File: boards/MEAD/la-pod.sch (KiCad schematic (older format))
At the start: 22 parts, among them J1 CONN_SFF8087

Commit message: Continued MEAD layout
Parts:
- removed TP4: TESTPAD, azonenberg_pcb:TESTPOINT_SMT_0.5MM, symbol Connector:Conn_01x01
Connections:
- net GND: now also TP12.1 (Pin_1)
- net TX0_N: now also J1.B2 (TX0_P); no longer J1.B3 (TX0_N)
- net TX0_P: now also J1.B3 (TX0_N); no longer J1.B2 (TX0_P)
- net TX1_N: now also D2.1 (IO1); no longer D2.3 (IO2)
- net TX1_P: now also D2.3 (IO2); no longer D2.1 (IO1)
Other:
- note added: "Invert lanes 0 for routability"
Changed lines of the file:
@@
 Text Label 4800 2600 2    50   ~ 0
 5V0
-Wire Wire Line
-	7700 1200 8250 1200
-Wire Wire Line
-	7700 1300 8250 1300
 $Comp
 L special-azonenberg:SP4010 D1
@@
 Wire Wire Line
 	7700 1600 8250 1600
-Text Label 7800 1200 0    50   ~ 0
+Text Label 7700 1200 0    50   ~ 0
 TX0_P
-Text Label 7800 1300 0    50   ~ 0
+Text Label 7700 1300 0    50   ~ 0
 TX0_N
 Text Label 7800 1500 0    50   ~ 0
@@
 	1    0    0    -1
 $EndComp
+Text Label 900  7450 2    50   ~ 0
+TX1_P
 Text Label 900  7350 2    50   ~ 0
-TX1_P
-Text Label 900  7450 2    50   ~ 0
 TX1_N
 Text Label 900  6850 2    50   ~ 0
@@
 	1    0    0    -1
 $EndComp
-Text Label 9700 5400 2    50   ~ 0
-GND
-$Comp
-L Connector:Conn_01x01 TP4
-U 1 1 5ED5A825
-P 8950 5200
-F 0 "TP4" H 9030 5242 50  0000 L CNN
-F 1 "TESTPAD" H 9030 5151 50  0000 L CNN
-F 2 "azonenberg_pcb:TESTPOINT_SMT_0.5MM" H 8950 5200 50  0001 C CNN
-F 3 "~" H 8950 5200 50  0001 C CNN
-	1    8950 5200
-	1    0    0    -1
-$EndComp
-Text Label 8750 5200 2    50   ~ 0
-12V0
+Text Label 9700 5450 2    50   ~ 0
+GND
 $Comp
 L Connector:Conn_01x01 TP5
@@
 	1    0    0    -1
 $EndComp
+Text Label 8250 1300 2    50   ~ 0
+TX0_P
+Text Label 8250 1200 2    50   ~ 0
+TX0_N
+Text Notes 8350 1100 0    50   ~ 0
+Invert lanes 0 for routability
 $EndSCHEMATC

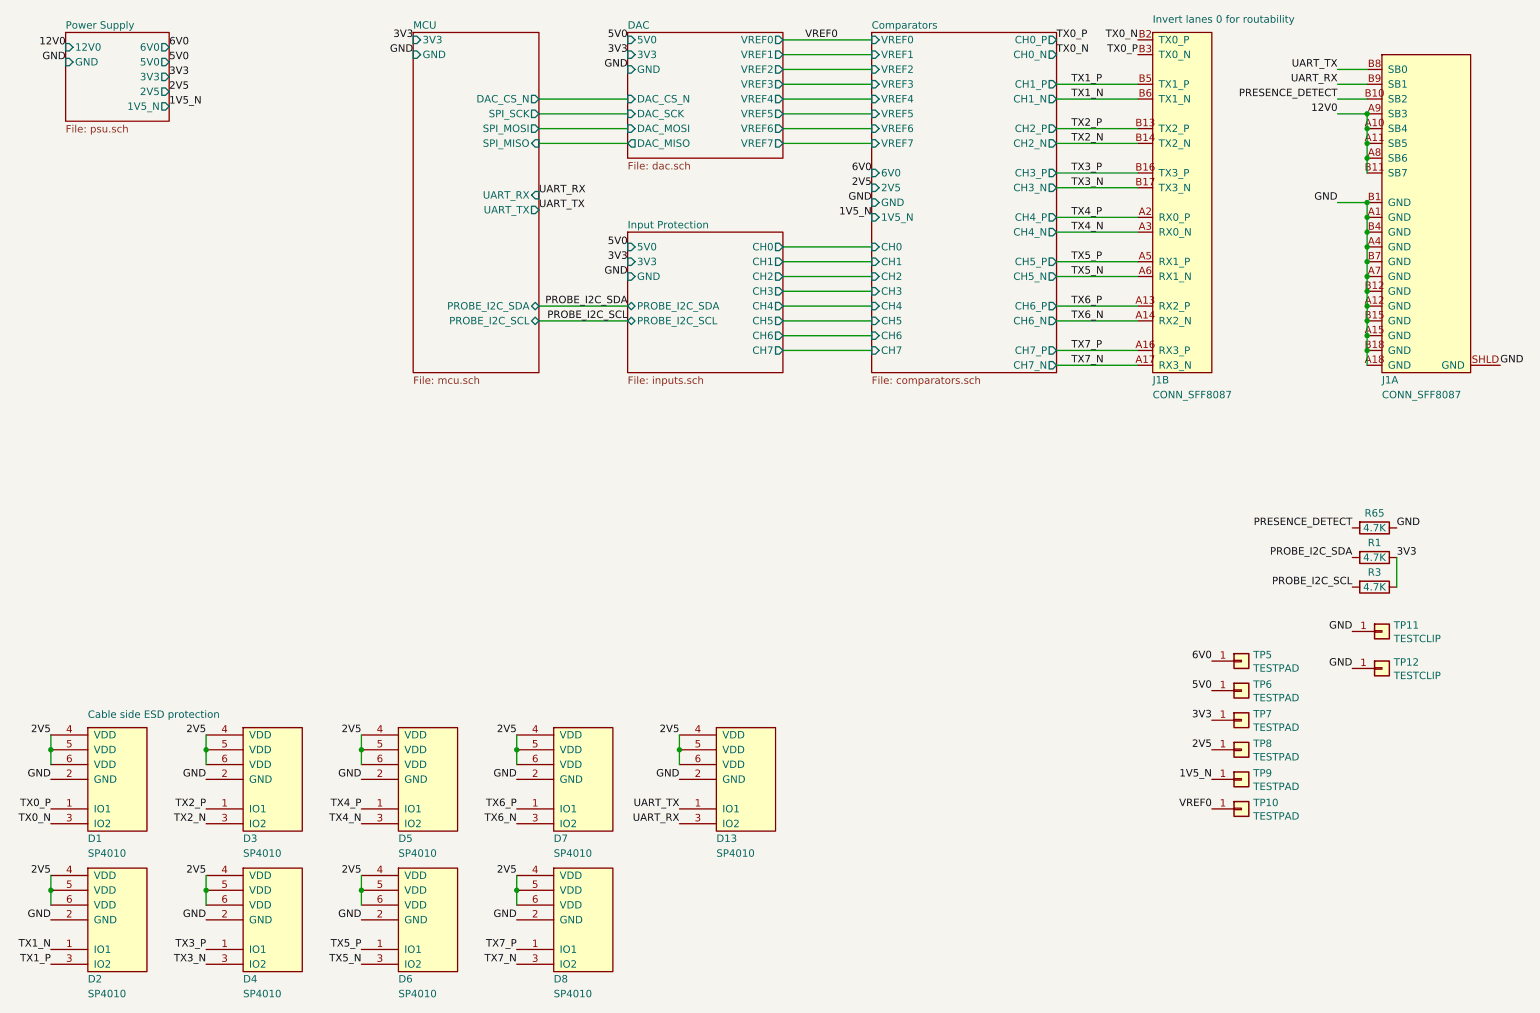
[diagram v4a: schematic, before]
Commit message: Continued MEAD layout. Right side is almost done.
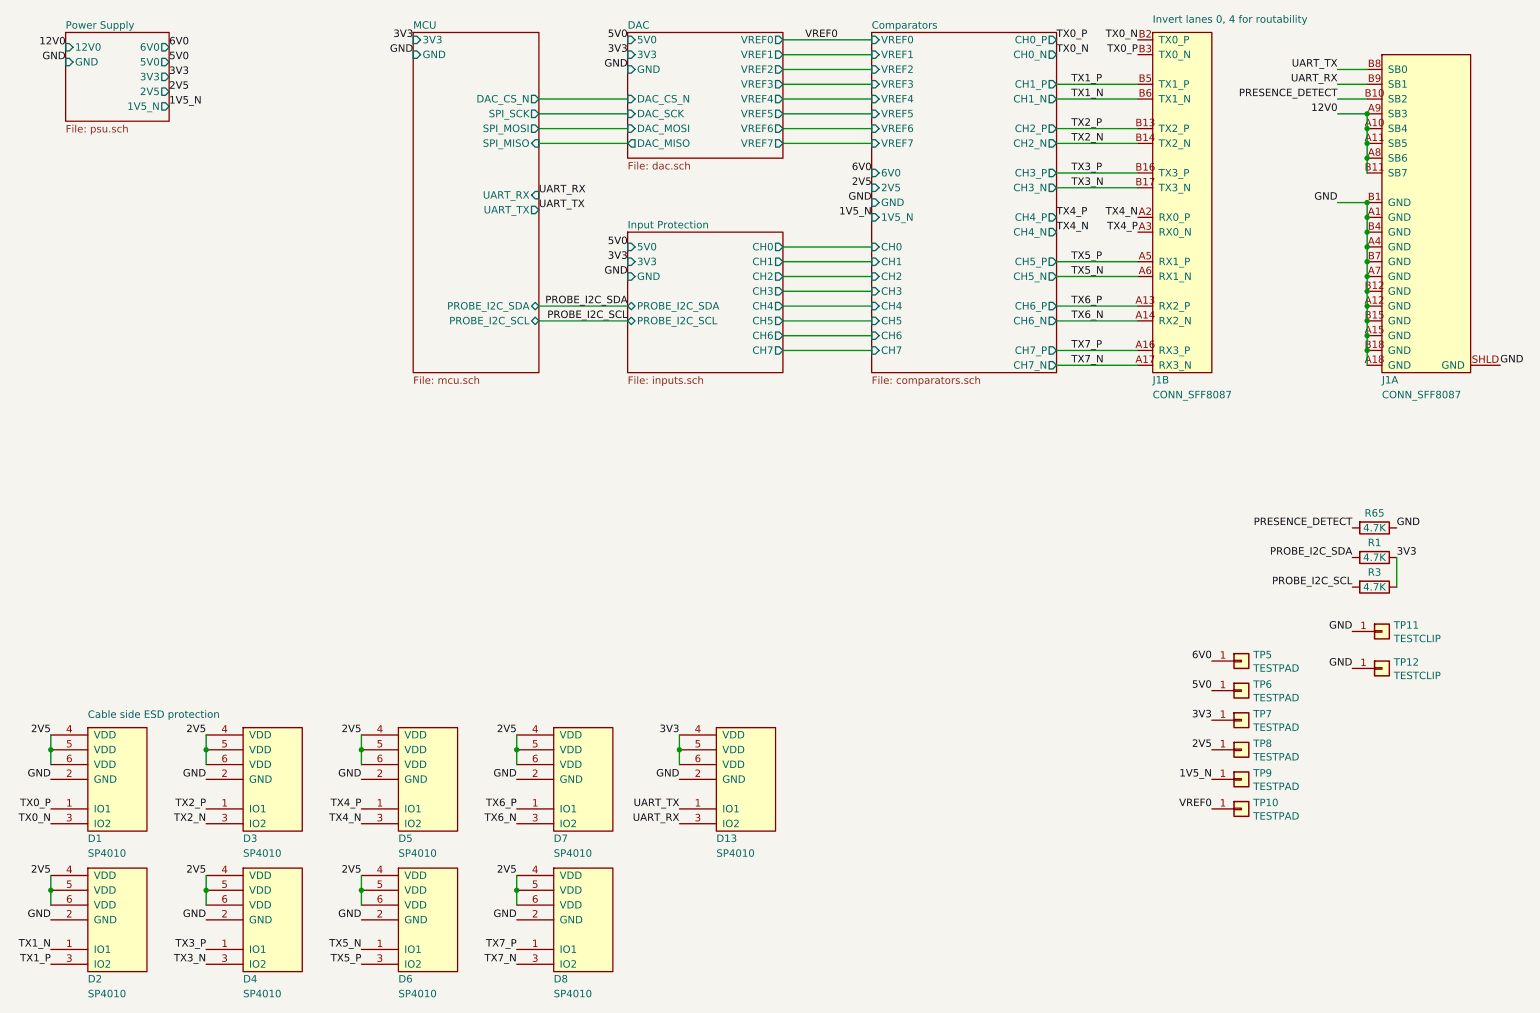
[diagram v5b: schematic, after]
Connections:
- net 2V5: no longer D13.4 (VDD), D13.5 (VDD), D13.6 (VDD)
- net 3V3: now also D13.4 (VDD), D13.5 (VDD), D13.6 (VDD)
- net TX4_N: now also J1.A2 (RX0_P); no longer J1.A3 (RX0_N)
- net TX4_P: now also J1.A3 (RX0_N); no longer J1.A2 (RX0_P)
- net TX5_N: now also D6.1 (IO1); no longer D6.3 (IO2)
- net TX5_P: now also D6.3 (IO2); no longer D6.1 (IO1)
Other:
- note added: "Invert lanes 0, 4 for routability"
- note removed: "Invert lanes 0 for routability"
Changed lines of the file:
@@
 Wire Wire Line
 	7700 2200 8250 2200
-Text Label 7800 2400 0    50   ~ 0
+Text Label 7700 2400 0    50   ~ 0
 TX4_P
-Text Label 7800 2500 0    50   ~ 0
+Text Label 7700 2500 0    50   ~ 0
 TX4_N
-Wire Wire Line
-	7700 2400 8250 2400
-Wire Wire Line
-	7700 2500 8250 2500
 Text Label 7800 2700 0    50   ~ 0
 TX5_P
@@
 	1    0    0    -1
 $EndComp
+Text Label 3000 7450 2    50   ~ 0
+TX5_P
 Text Label 3000 7350 2    50   ~ 0
-TX5_P
-Text Label 3000 7450 2    50   ~ 0
 TX5_N
 Text Label 3000 6850 2    50   ~ 0
@@
 $EndComp
 Text Label 5150 5900 2    50   ~ 0
-2V5
+3V3
 Wire Wire Line
 	5150 5900 5150 6000
@@
 TX0_N
 Text Notes 8350 1100 0    50   ~ 0
-Invert lanes 0 for routability
+Invert lanes 0, 4 for routability
+Text Label 8250 2500 2    50   ~ 0
+TX4_P
+Text Label 8250 2400 2    50   ~ 0
+TX4_N
 $EndSCHEMATC

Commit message: Finished MCU layout, began left side comparator layout.
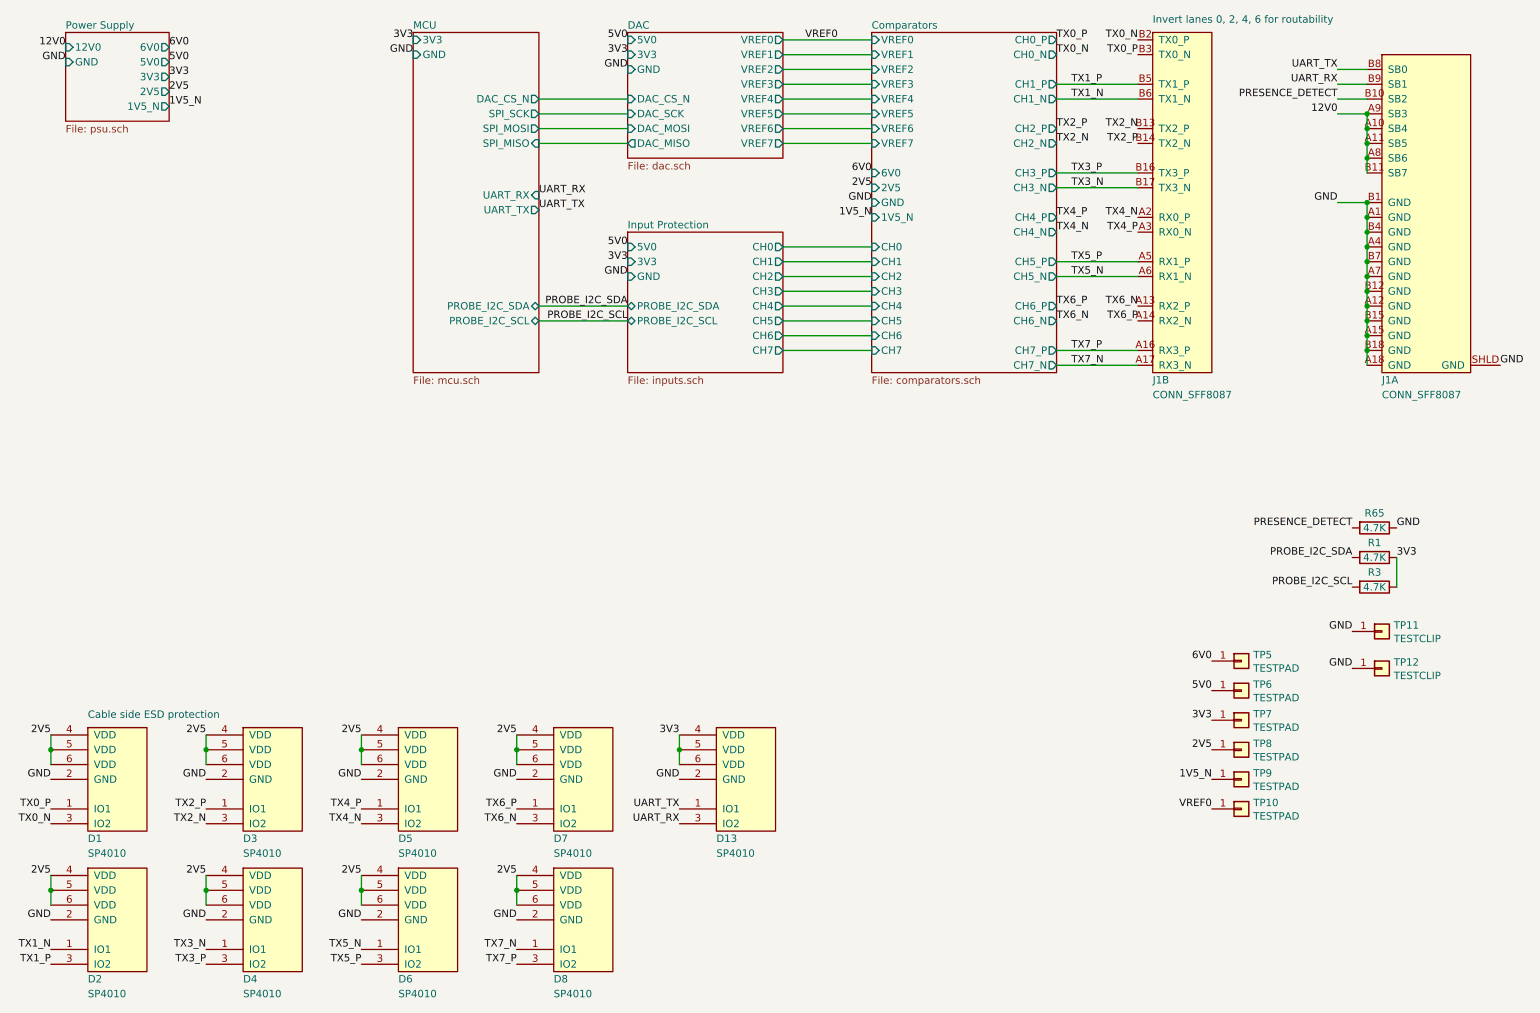
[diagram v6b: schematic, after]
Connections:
- net TX2_N: now also J1.B13 (TX2_P); no longer J1.B14 (TX2_N)
- net TX2_P: now also J1.B14 (TX2_N); no longer J1.B13 (TX2_P)
- net TX3_N: now also D4.1 (IO1); no longer D4.3 (IO2)
- net TX3_P: now also D4.3 (IO2); no longer D4.1 (IO1)
- net TX6_N: now also J1.A13 (RX2_P); no longer J1.A14 (RX2_N)
- net TX6_P: now also J1.A14 (RX2_N); no longer J1.A13 (RX2_P)
- net TX7_N: now also D8.1 (IO1); no longer D8.3 (IO2)
- net TX7_P: now also D8.3 (IO2); no longer D8.1 (IO1)
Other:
- note added: "Invert lanes 0, 2, 4, 6 for routability"
- note removed: "Invert lanes 0, 4 for routability"
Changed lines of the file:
@@
 	1    0    0    -1
 $EndComp
-Wire Wire Line
-	7700 1500 8250 1500
-Wire Wire Line
-	7700 1600 8250 1600
 Text Label 7700 1200 0    50   ~ 0
 TX0_P
@@
 Text Label 7800 1600 0    50   ~ 0
 TX1_N
-Text Label 7800 1800 0    50   ~ 0
+Text Label 7700 1800 0    50   ~ 0
 TX2_P
-Text Label 7800 1900 0    50   ~ 0
+Text Label 7700 1900 0    50   ~ 0
 TX2_N
 Text Label 7800 2100 0    50   ~ 0
@@
 Text Label 7800 2200 0    50   ~ 0
 TX3_N
-Wire Wire Line
-	7700 1800 8250 1800
-Wire Wire Line
-	7700 1900 8250 1900
-Wire Wire Line
-	7700 2100 8250 2100
-Wire Wire Line
-	7700 2200 8250 2200
 Text Label 7700 2400 0    50   ~ 0
 TX4_P
@@
 Wire Wire Line
 	7700 2800 8250 2800
-Text Label 7800 3000 0    50   ~ 0
+Text Label 7700 3000 0    50   ~ 0
 TX6_P
-Text Label 7800 3100 0    50   ~ 0
+Text Label 7700 3100 0    50   ~ 0
 TX6_N
-Wire Wire Line
-	7700 3000 8250 3000
-Wire Wire Line
-	7700 3100 8250 3100
 Text Label 7800 3300 0    50   ~ 0
 TX7_P
@@
 	1    0    0    -1
 $EndComp
+Text Label 1950 7450 2    50   ~ 0
+TX3_P
 Text Label 1950 7350 2    50   ~ 0
-TX3_P
-Text Label 1950 7450 2    50   ~ 0
 TX3_N
 Text Label 1950 6850 2    50   ~ 0
@@
 	1    0    0    -1
 $EndComp
+Text Label 4050 7450 2    50   ~ 0
+TX7_P
 Text Label 4050 7350 2    50   ~ 0
-TX7_P
-Text Label 4050 7450 2    50   ~ 0
 TX7_N
 Text Label 4050 6850 2    50   ~ 0
@@
 TX0_N
 Text Notes 8350 1100 0    50   ~ 0
-Invert lanes 0, 4 for routability
+Invert lanes 0, 2, 4, 6 for routability
 Text Label 8250 2500 2    50   ~ 0
 TX4_P
 Text Label 8250 2400 2    50   ~ 0
 TX4_N
+Wire Wire Line
+	7700 1600 8250 1600
+Wire Wire Line
+	7700 1500 8250 1500
+Text Label 8250 3100 2    50   ~ 0
+TX6_P
+Text Label 8250 3000 2    50   ~ 0
+TX6_N
+Text Label 8250 1900 2    50   ~ 0
+TX2_P
+Text Label 8250 1800 2    50   ~ 0
+TX2_N
+Wire Wire Line
+	7700 2100 8250 2100
+Wire Wire Line
+	7700 2200 8250 2200
 $EndSCHEMATC

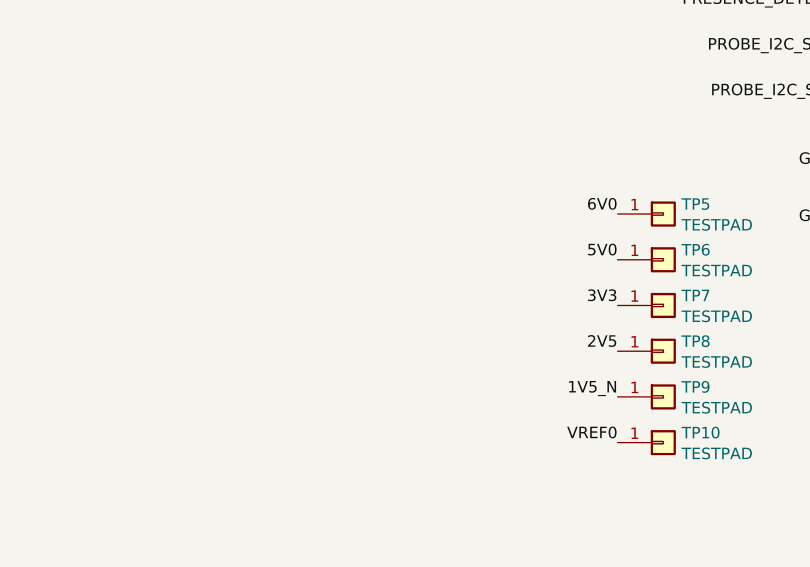
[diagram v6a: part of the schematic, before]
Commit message: Continued layout on MEAD. All comparators done, LVDS length matched, DAC routed
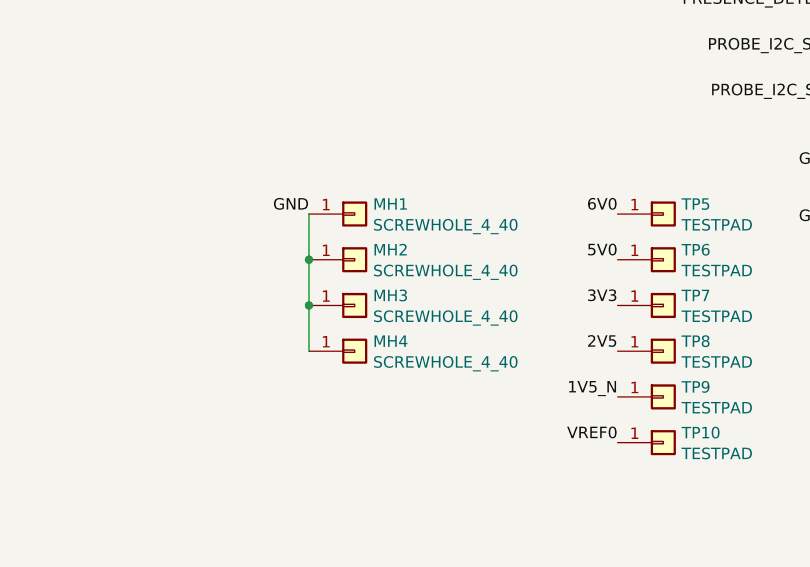
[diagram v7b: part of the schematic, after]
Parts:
- added MH1, MH2, MH3, MH4: SCREWHOLE_4_40, azonenberg_pcb:MECHANICAL_CLEARANCEHOLE_4_40, symbol Connector:Conn_01x01
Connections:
- net GND: now also MH1.1 (Pin_1), MH2.1 (Pin_1), MH3.1 (Pin_1), MH4.1 (Pin_1)
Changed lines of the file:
@@
 Wire Wire Line
 	7700 2200 8250 2200
+$Comp
+L Connector:Conn_01x01 MH1
+U 1 1 5F2DE5BB
+P 7600 5400
+F 0 "MH1" H 7680 5442 50  0000 L CNN
+F 1 "SCREWHOLE_4_40" H 7680 5351 50  0000 L CNN
+F 2 "azonenberg_pcb:MECHANICAL_CLEARANCEHOLE_4_40" H 7600 5400 50  0001 C CNN
+F 3 "~" H 7600 5400 50  0001 C CNN
+	1    7600 5400
+	1    0    0    -1
+$EndComp
+Text Label 7400 5400 2    50   ~ 0
+GND
+$Comp
+L Connector:Conn_01x01 MH2
+U 1 1 5F2DF305
+P 7600 5600
+F 0 "MH2" H 7680 5642 50  0000 L CNN
+F 1 "SCREWHOLE_4_40" H 7680 5551 50  0000 L CNN
+F 2 "azonenberg_pcb:MECHANICAL_CLEARANCEHOLE_4_40" H 7600 5600 50  0001 C CNN
+F 3 "~" H 7600 5600 50  0001 C CNN
+	1    7600 5600
+	1    0    0    -1
+$EndComp
+$Comp
+L Connector:Conn_01x01 MH3
+U 1 1 5F2DF699
+P 7600 5800
+F 0 "MH3" H 7680 5842 50  0000 L CNN
+F 1 "SCREWHOLE_4_40" H 7680 5751 50  0000 L CNN
+F 2 "azonenberg_pcb:MECHANICAL_CLEARANCEHOLE_4_40" H 7600 5800 50  0001 C CNN
+F 3 "~" H 7600 5800 50  0001 C CNN
+	1    7600 5800
+	1    0    0    -1
+$EndComp
+$Comp
+L Connector:Conn_01x01 MH4
+U 1 1 5F2DFA38
+P 7600 6000
+F 0 "MH4" H 7680 6042 50  0000 L CNN
+F 1 "SCREWHOLE_4_40" H 7680 5951 50  0000 L CNN
+F 2 "azonenberg_pcb:MECHANICAL_CLEARANCEHOLE_4_40" H 7600 6000 50  0001 C CNN
+F 3 "~" H 7600 6000 50  0001 C CNN
+	1    7600 6000
+	1    0    0    -1
+$EndComp
+Wire Wire Line
+	7400 6000 7400 5800
+Connection ~ 7400 5600
+Wire Wire Line
+	7400 5600 7400 5400
+Connection ~ 7400 5800
+Wire Wire Line
+	7400 5800 7400 5600
 $EndSCHEMATC

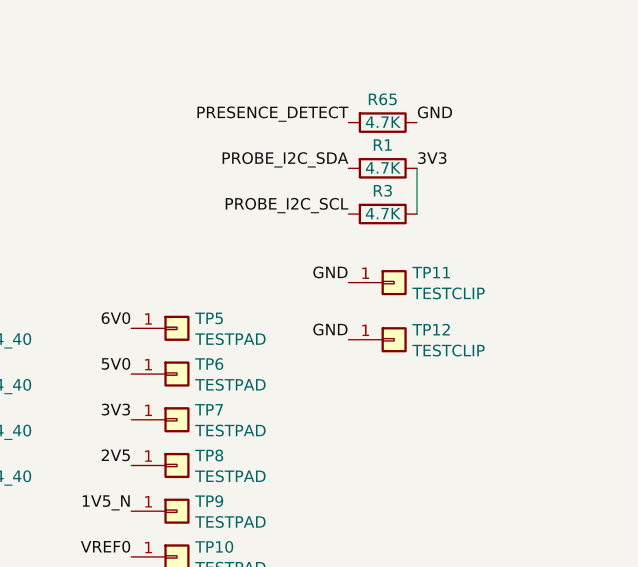
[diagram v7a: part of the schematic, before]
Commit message: Updating file: la-pod.kicad_pcb with current fully routed design
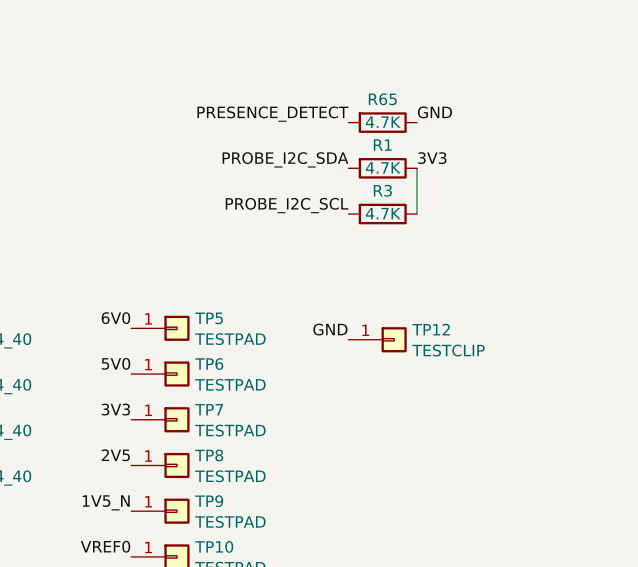
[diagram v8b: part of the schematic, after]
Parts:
- removed TP11: TESTCLIP, azonenberg_pcb:TESTPOINT_SMT_KEYSTONE_5016, symbol Connector:Conn_01x01
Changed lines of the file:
@@
 Sheet 1 6
 Title "Logic Analyzer Pod"
-Date "2020-05-29"
+Date "2020-05-30"
 Rev "0.1"
 Comp "Antikernel Labs"
@@
 UART_RX
 $Comp
-L Connector:Conn_01x01 TP11
-U 1 1 5ED596F2
-P 9900 5200
-F 0 "TP11" H 9980 5242 50  0000 L CNN
-F 1 "TESTCLIP" H 9980 5151 50  0000 L CNN
-F 2 "azonenberg_pcb:TESTPOINT_SMT_KEYSTONE_5016" H 9900 5200 50  0001 C CNN
-F 3 "~" H 9900 5200 50  0001 C CNN
-	1    9900 5200
-	1    0    0    -1
-$EndComp
-Text Label 9700 5200 2    50   ~ 0
-GND
-$Comp
 L Connector:Conn_01x01 TP12
